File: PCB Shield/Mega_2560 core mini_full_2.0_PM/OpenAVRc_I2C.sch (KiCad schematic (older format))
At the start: 12 parts, among them P15 LCD_I2C, P2 Clock, P3 Option, U7 FM24W256, U8 DS3231SN

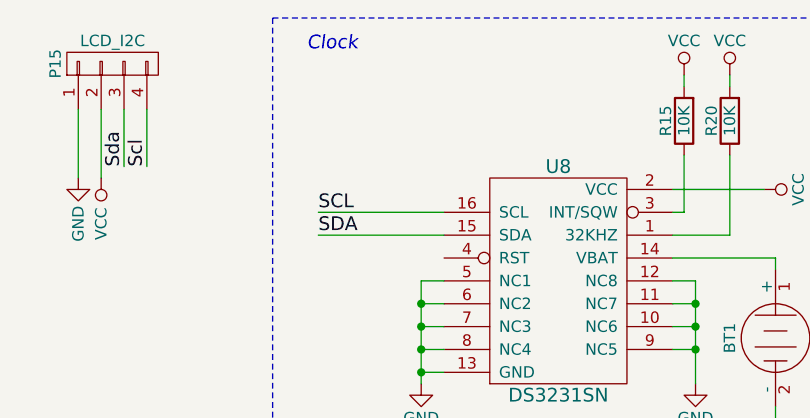
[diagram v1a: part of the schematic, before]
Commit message: Update pcb shield (add 2 resistors on I2C bus)
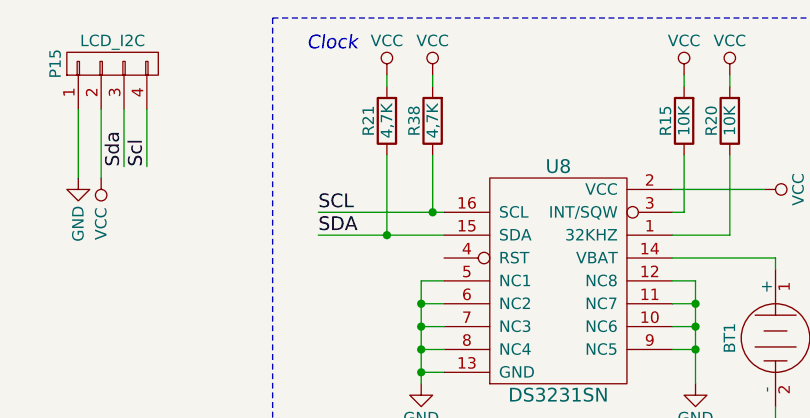
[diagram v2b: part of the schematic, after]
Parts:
- added R21, R38: 4,7K, Resistors_SMD:R_1206, symbol R-RESCUE-Mega_2560_core_mini_full_2.0
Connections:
- net SCL: now also R38.1
- net SDA: now also R21.1
- net VCC: now also R21.2, R38.2
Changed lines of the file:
@@
 $EndComp
 $Comp
-L GND-RESCUE-Mega_2560_core_mini_full_2.0 #PWR082
+L GND-RESCUE-Mega_2560_core_mini_full_2.0 #PWR98
 U 1 1 59C56715
 P 8250 4650
-F 0 "#PWR082" H 8250 4400 50  0001 C CNN
+F 0 "#PWR98" H 8250 4400 50  0001 C CNN
 F 1 "GND" H 8250 4500 50  0000 C CNN
 F 2 "" H 8250 4650 50  0000 C CNN
@@
 $EndComp
 $Comp
-L VCC #PWR083
+L VCC #PWR97
 U 1 1 59C5671B
 P 8250 3350
-F 0 "#PWR083" H 8250 3200 50  0001 C CNN
+F 0 "#PWR97" H 8250 3200 50  0001 C CNN
 F 1 "VCC" H 8250 3500 50  0000 C CNN
 F 2 "" H 8250 3350 50  0000 C CNN
@@
 $EndComp
 $Comp
-L GND-RESCUE-Mega_2560_core_mini_full_2.0 #PWR084
+L GND-RESCUE-Mega_2560_core_mini_full_2.0 #PWR99
 U 1 1 59C56728
 P 8700 3450
-F 0 "#PWR084" H 8700 3200 50  0001 C CNN
+F 0 "#PWR99" H 8700 3200 50  0001 C CNN
 F 1 "GND" H 8700 3300 50  0000 C CNN
 F 2 "" H 8700 3450 50  0000 C CNN
@@
 Sda
 $Comp
-L GND-RESCUE-Mega_2560_core_mini_full_2.0 #PWR085
+L GND-RESCUE-Mega_2560_core_mini_full_2.0 #PWR100
 U 1 1 59C56730
 P 9050 3950
-F 0 "#PWR085" H 9050 3700 50  0001 C CNN
+F 0 "#PWR100" H 9050 3700 50  0001 C CNN
 F 1 "GND" H 9050 3800 50  0000 C CNN
 F 2 "" H 9050 3950 50  0000 C CNN
@@
 $EndComp
 $Comp
-L GND-RESCUE-Mega_2560_core_mini_full_2.0 #PWR086
+L GND-RESCUE-Mega_2560_core_mini_full_2.0 #PWR87
 U 1 1 59C5673F
 P 4550 4600
-F 0 "#PWR086" H 4550 4350 50  0001 C CNN
+F 0 "#PWR87" H 4550 4350 50  0001 C CNN
 F 1 "GND" H 4550 4450 50  0000 C CNN
 F 2 "" H 4550 4600 50  0000 C CNN
@@
 $EndComp
 $Comp
-L GND-RESCUE-Mega_2560_core_mini_full_2.0 #PWR087
+L GND-RESCUE-Mega_2560_core_mini_full_2.0 #PWR90
 U 1 1 59C56745
 P 5750 4600
-F 0 "#PWR087" H 5750 4350 50  0001 C CNN
+F 0 "#PWR90" H 5750 4350 50  0001 C CNN
 F 1 "GND" H 5750 4450 50  0000 C CNN
 F 2 "" H 5750 4600 50  0000 C CNN
@@
 $EndComp
 $Comp
-L GND-RESCUE-Mega_2560_core_mini_full_2.0 #PWR088
+L GND-RESCUE-Mega_2560_core_mini_full_2.0 #PWR93
 U 1 1 59C5674B
 P 6100 4800
-F 0 "#PWR088" H 6100 4550 50  0001 C CNN
+F 0 "#PWR93" H 6100 4550 50  0001 C CNN
 F 1 "GND" H 6100 4650 50  0000 C CNN
 F 2 "" H 6100 4800 50  0000 C CNN
@@
 $EndComp
 $Comp
-L VCC #PWR089
+L VCC #PWR94
 U 1 1 59C56758
 P 6350 3250
-F 0 "#PWR089" H 6350 3100 50  0001 C CNN
+F 0 "#PWR94" H 6350 3100 50  0001 C CNN
 F 1 "VCC" H 6350 3400 50  0000 C CNN
 F 2 "" H 6350 3250 50  0000 C CNN
@@
 $EndComp
 $Comp
-L GND-RESCUE-Mega_2560_core_mini_full_2.0 #PWR090
+L GND-RESCUE-Mega_2560_core_mini_full_2.0 #PWR95
 U 1 1 59C5675E
 P 6350 3650
-F 0 "#PWR090" H 6350 3400 50  0001 C CNN
+F 0 "#PWR95" H 6350 3400 50  0001 C CNN
 F 1 "GND" H 6350 3500 50  0000 C CNN
 F 2 "" H 6350 3650 50  0000 C CNN
@@
 $EndComp
 $Comp
-L VCC #PWR091
+L VCC #PWR92
 U 1 1 59C56764
 P 6050 3750
-F 0 "#PWR091" H 6050 3600 50  0001 C CNN
+F 0 "#PWR92" H 6050 3600 50  0001 C CNN
 F 1 "VCC" H 6050 3900 50  0000 C CNN
 F 2 "" H 6050 3750 50  0000 C CNN
@@
 $EndComp
 $Comp
-L VCC #PWR092
+L VCC #PWR91
 U 1 1 59C56778
 P 5900 3250
-F 0 "#PWR092" H 5900 3100 50  0001 C CNN
+F 0 "#PWR91" H 5900 3100 50  0001 C CNN
 F 1 "VCC" H 5900 3400 50  0000 C CNN
 F 2 "" H 5900 3250 50  0000 C CNN
@@
 $EndComp
 $Comp
-L VCC #PWR093
+L VCC #PWR89
 U 1 1 59C5677E
 P 5700 3250
-F 0 "#PWR093" H 5700 3100 50  0001 C CNN
+F 0 "#PWR89" H 5700 3100 50  0001 C CNN
 F 1 "VCC" H 5700 3400 50  0000 C CNN
 F 2 "" H 5700 3250 50  0000 C CNN
@@
 $EndComp
 $Comp
-L GND-RESCUE-Mega_2560_core_mini_full_2.0 #PWR094
+L GND-RESCUE-Mega_2560_core_mini_full_2.0 #PWR96
 U 1 1 59C56784
 P 7450 4150
-F 0 "#PWR094" H 7450 3900 50  0001 C CNN
+F 0 "#PWR96" H 7450 3900 50  0001 C CNN
 F 1 "GND" H 7450 4000 50  0000 C CNN
 F 2 "" H 7450 4150 50  0000 C CNN
@@
 	7050 5000 7050 3000
 $Comp
-L VCC #PWR095
+L VCC #PWR80
 U 1 1 59C57848
 P 2250 3800
-F 0 "#PWR095" H 2250 3650 50  0001 C CNN
+F 0 "#PWR80" H 2250 3650 50  0001 C CNN
 F 1 "VCC" H 2250 3950 50  0000 C CNN
 F 2 "" H 2250 3800 50  0000 C CNN
@@
 $EndComp
 $Comp
-L GND-RESCUE-Mega_2560_core_mini_full_2.0 #PWR096
+L GND-RESCUE-Mega_2560_core_mini_full_2.0 #PWR82
 U 1 1 59C5784E
 P 2550 3800
-F 0 "#PWR096" H 2550 3550 50  0001 C CNN
+F 0 "#PWR82" H 2550 3550 50  0001 C CNN
 F 1 "GND" H 2550 3650 50  0000 C CNN
 F 2 "" H 2550 3800 50  0000 C CNN
@@
 $EndComp
 $Comp
-L GND-RESCUE-Mega_2560_core_mini_full_2.0 #PWR097
+L GND-RESCUE-Mega_2560_core_mini_full_2.0 #PWR84
 U 1 1 59C57864
 P 3050 3700
-F 0 "#PWR097" H 3050 3450 50  0001 C CNN
+F 0 "#PWR84" H 3050 3450 50  0001 C CNN
 F 1 "GND" V 3050 3500 50  0000 C CNN
 F 2 "" H 3050 3700 50  0000 C CNN
@@
 Scl
 $Comp
-L VCC #PWR098
+L VCC #PWR81
 U 1 1 59C5786C
 P 2250 4800
-F 0 "#PWR098" H 2250 4650 50  0001 C CNN
+F 0 "#PWR81" H 2250 4650 50  0001 C CNN
 F 1 "VCC" H 2250 4950 50  0000 C CNN
 F 2 "" H 2250 4800 50  0000 C CNN
@@
 $EndComp
 $Comp
-L GND-RESCUE-Mega_2560_core_mini_full_2.0 #PWR099
+L GND-RESCUE-Mega_2560_core_mini_full_2.0 #PWR83
 U 1 1 59C57872
 P 2550 4800
-F 0 "#PWR099" H 2550 4550 50  0001 C CNN
+F 0 "#PWR83" H 2550 4550 50  0001 C CNN
 F 1 "GND" H 2550 4650 50  0000 C CNN
 F 2 "" H 2550 4800 50  0000 C CNN
@@
 	3050 3400 3050 3700
 $Comp
-L VCC #PWR0100
+L VCC #PWR85
 U 1 1 59C578A5
 P 3150 3700
-F 0 "#PWR0100" H 3150 3550 50  0001 C CNN
+F 0 "#PWR85" H 3150 3550 50  0001 C CNN
 F 1 "VCC" V 3150 3900 50  0000 C CNN
 F 2 "" H 3150 3700 50  0000 C CNN
@@
 Text GLabel 1750 3550 0    60   BiDi ~ 0
 Sda
+$Comp
+L R-RESCUE-Mega_2560_core_mini_full_2.0 R21
+U 1 1 59D4D3D2
+P 4400 3450
+F 0 "R21" V 4480 3450 50  0000 C CNN
+F 1 "4,7K" V 4400 3450 50  0000 C CNN
+F 2 "Resistors_SMD:R_1206" V 4330 3450 50  0001 C CNN
+F 3 "" H 4400 3450 50  0000 C CNN
+	1    4400 3450
+	-1   0    0    1
+$EndComp
+$Comp
+L R-RESCUE-Mega_2560_core_mini_full_2.0 R38
+U 1 1 59D4D3D8
+P 4600 3450
+F 0 "R38" V 4680 3450 50  0000 C CNN
+F 1 "4,7K" V 4600 3450 50  0000 C CNN
+F 2 "Resistors_SMD:R_1206" V 4530 3450 50  0001 C CNN
+F 3 "" H 4600 3450 50  0000 C CNN
+	1    4600 3450
+	-1   0    0    1
+$EndComp
+$Comp
+L VCC #PWR88
+U 1 1 59D4D3DE
+P 4600 3250
+F 0 "#PWR88" H 4600 3100 50  0001 C CNN
+F 1 "VCC" H 4600 3400 50  0000 C CNN
+F 2 "" H 4600 3250 50  0000 C CNN
+F 3 "" H 4600 3250 50  0000 C CNN
+	1    4600 3250
+	1    0    0    -1
+$EndComp
+$Comp
+L VCC #PWR86
+U 1 1 59D4D3E4
+P 4400 3250
+F 0 "#PWR86" H 4400 3100 50  0001 C CNN
+F 1 "VCC" H 4400 3400 50  0000 C CNN
+F 2 "" H 4400 3250 50  0000 C CNN
+F 3 "" H 4400 3250 50  0000 C CNN
+	1    4400 3250
+	1    0    0    -1
+$EndComp
+Wire Wire Line
+	4400 3300 4400 3250
+Wire Wire Line
+	4600 3300 4600 3250
+Wire Wire Line
+	4600 3600 4600 3850
+Connection ~ 4600 3850
+Wire Wire Line
+	4400 3600 4400 3950
+Connection ~ 4400 3950
 $EndSCHEMATC
